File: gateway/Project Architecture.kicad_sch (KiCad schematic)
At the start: 0 parts

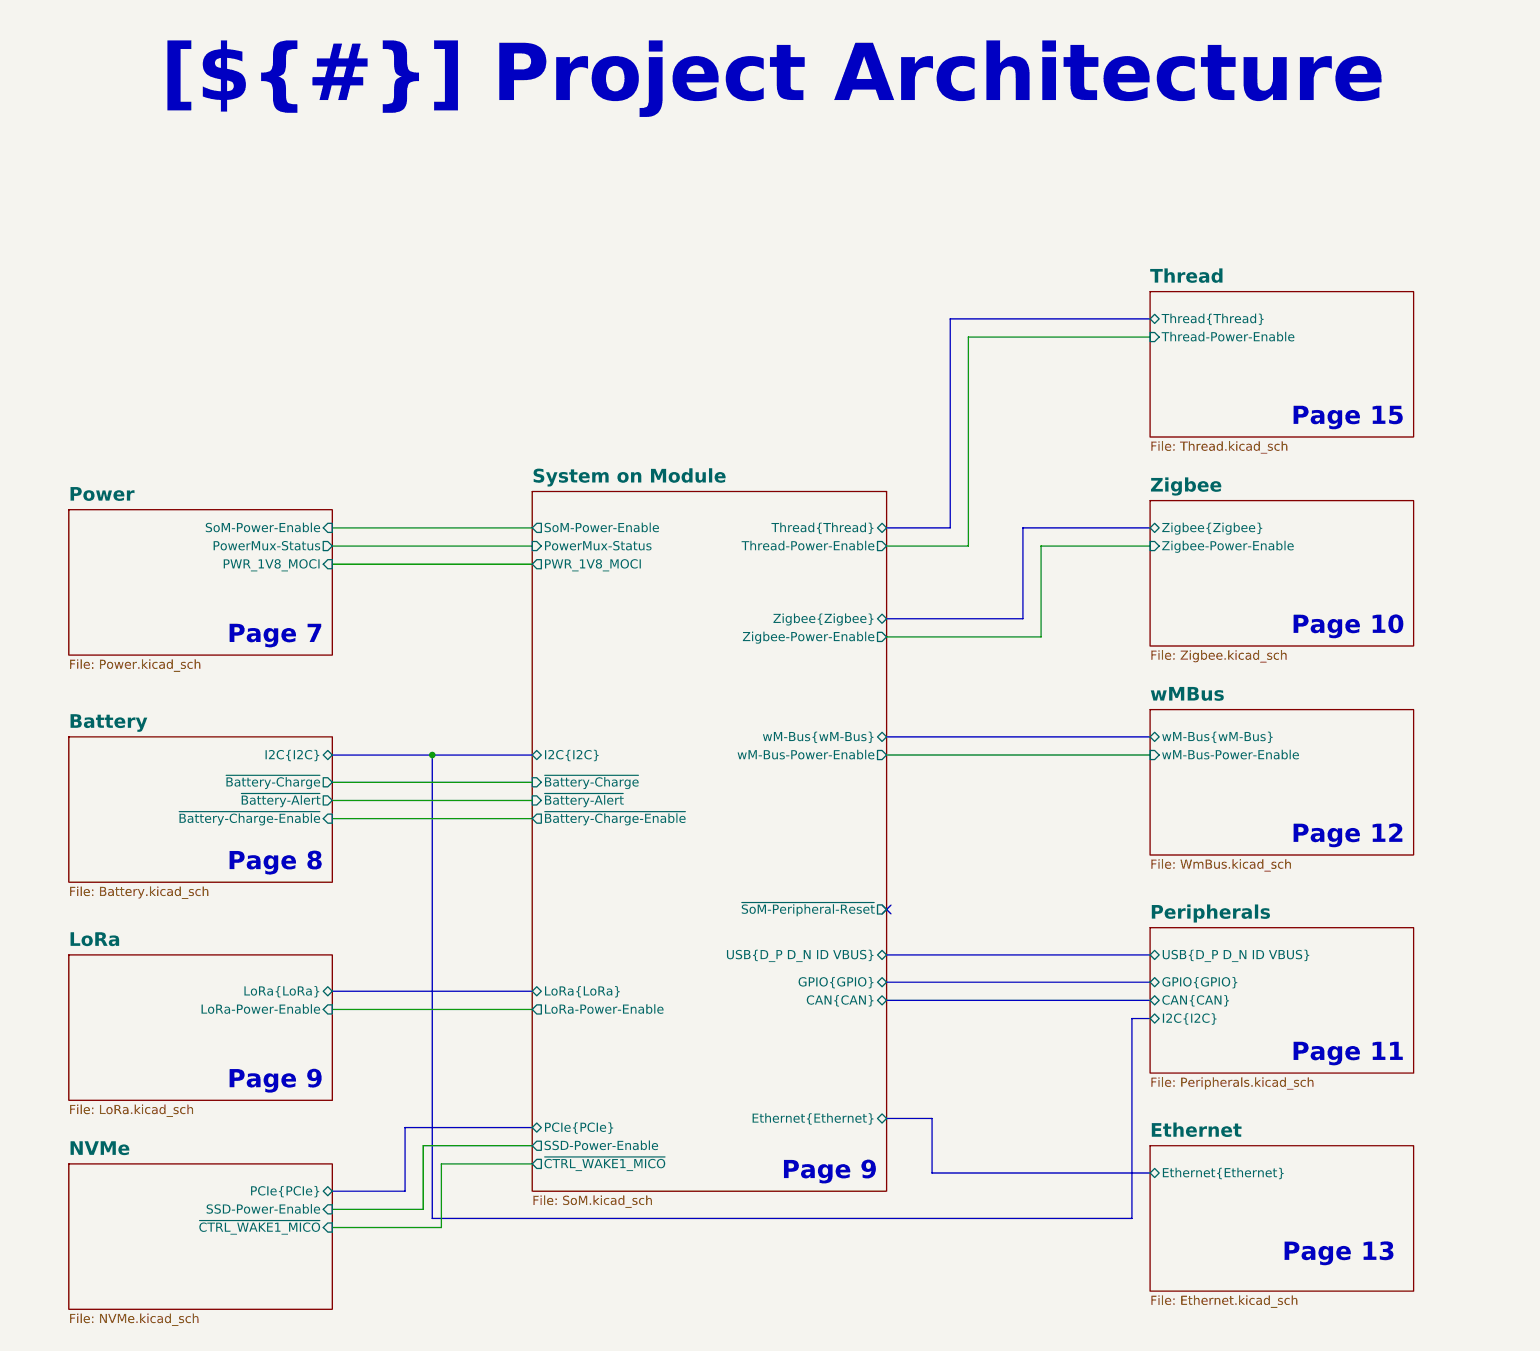
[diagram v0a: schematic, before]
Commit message: Add INA219 for current measurement
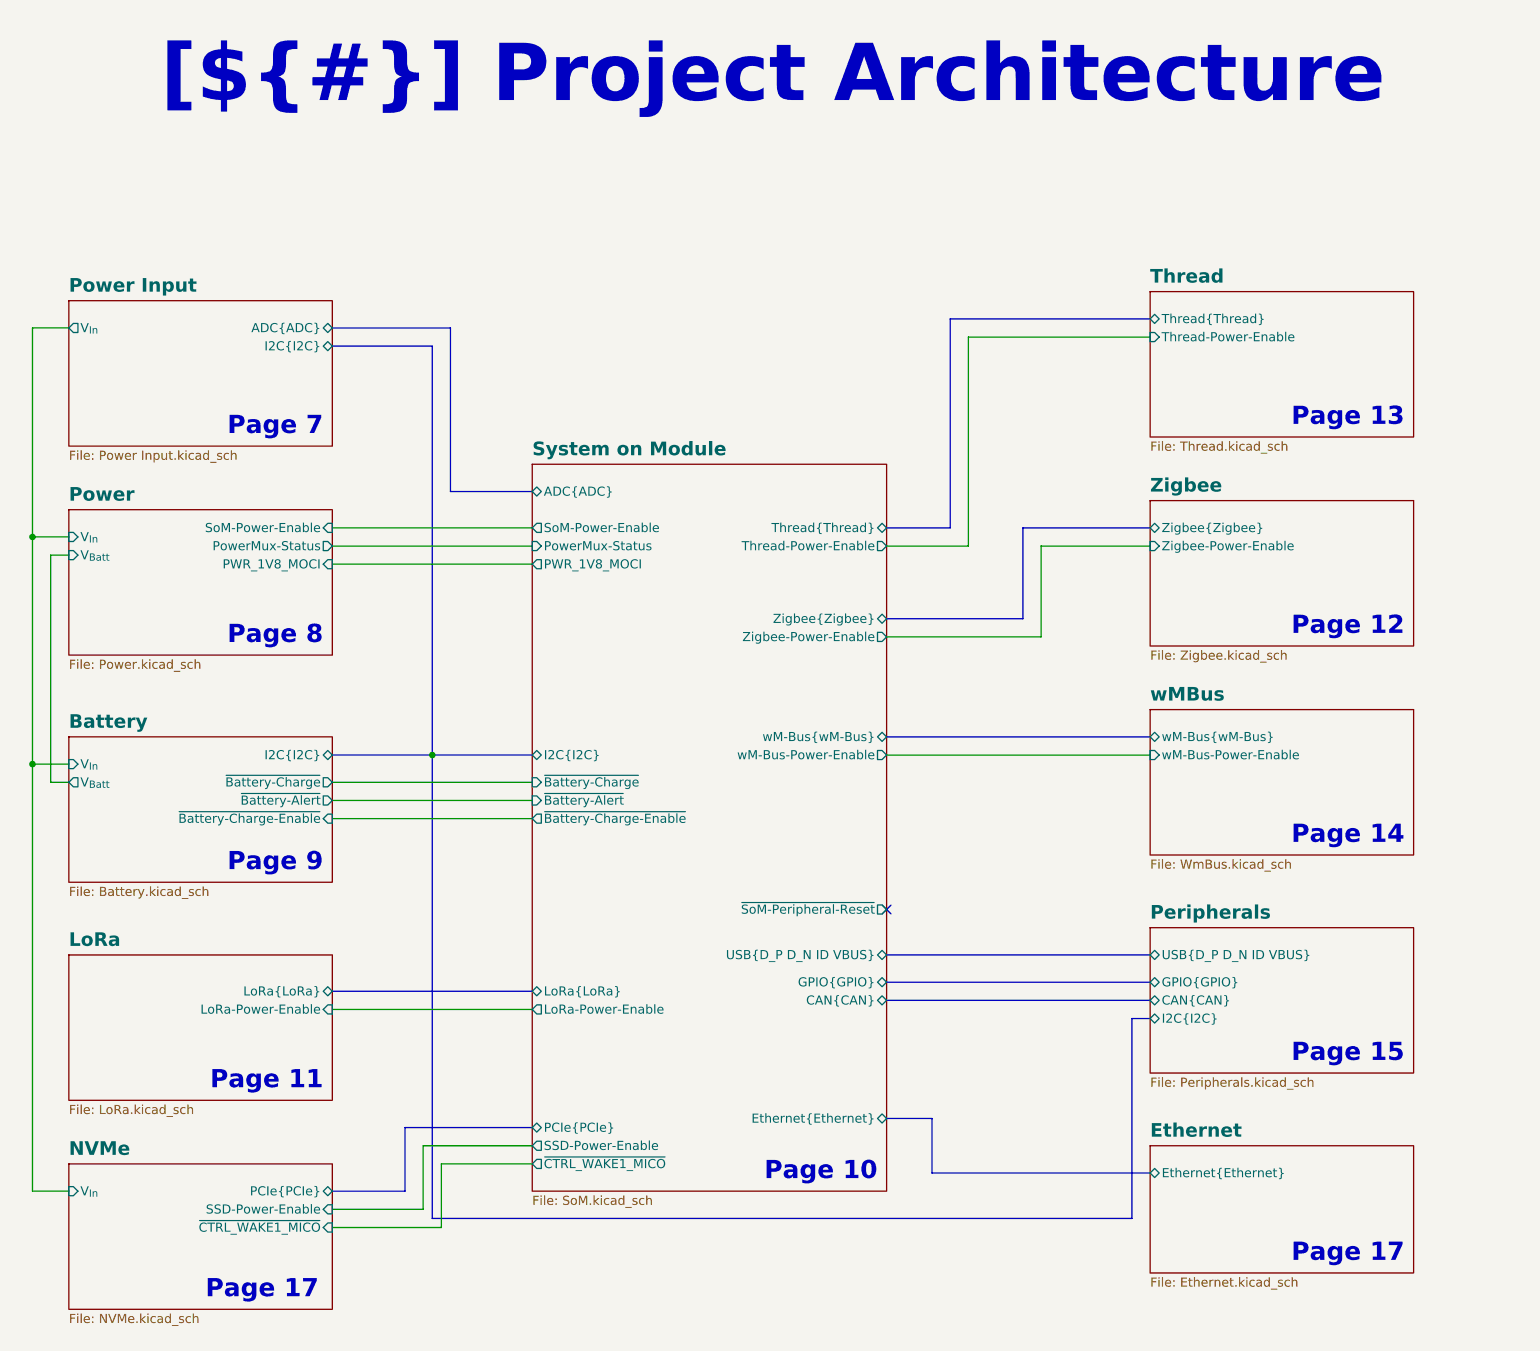
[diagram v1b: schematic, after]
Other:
- added sheet Power Input (Power Input.kicad_sch)
- sheet Battery ports: added V_{Batt}, V_{In}; removed none
- sheet NVMe ports: added V_{In}; removed none
- sheet Power ports: added V_{Batt}, V_{In}; removed none
- sheet System on Module ports: added ADC{ADC}; removed none
- note added: "Page 14"
- note added: "Page 17"

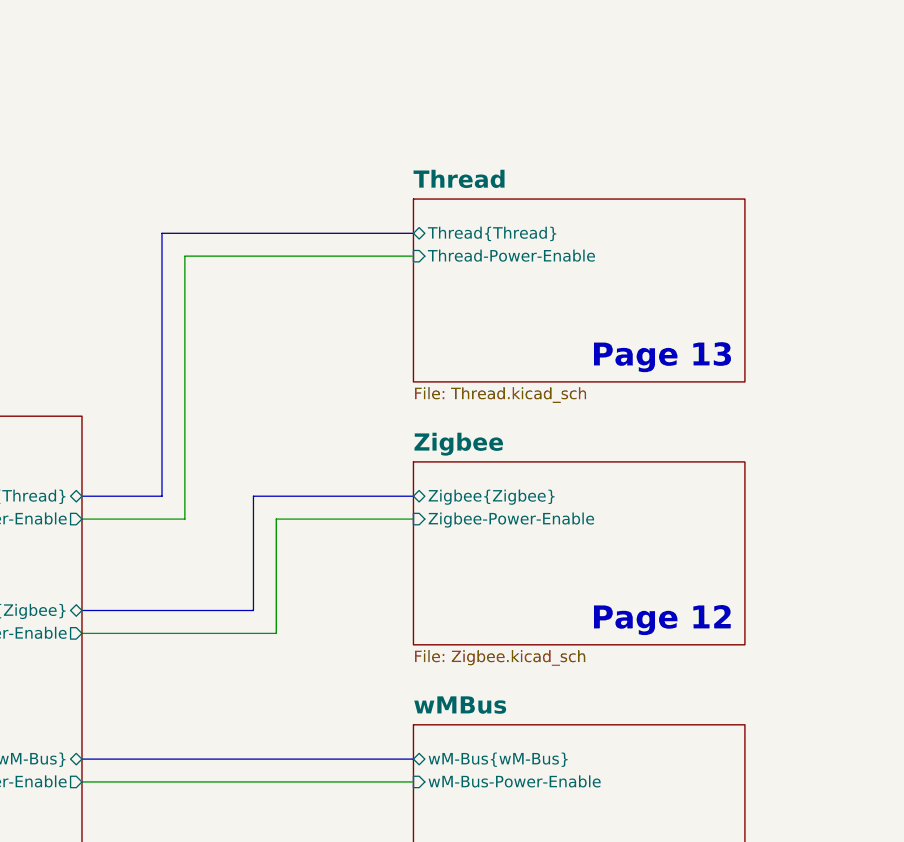
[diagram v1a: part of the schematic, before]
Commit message: Improving Thread
- Add boot signal for Thread MCU
- Add debug LED for nRF5340
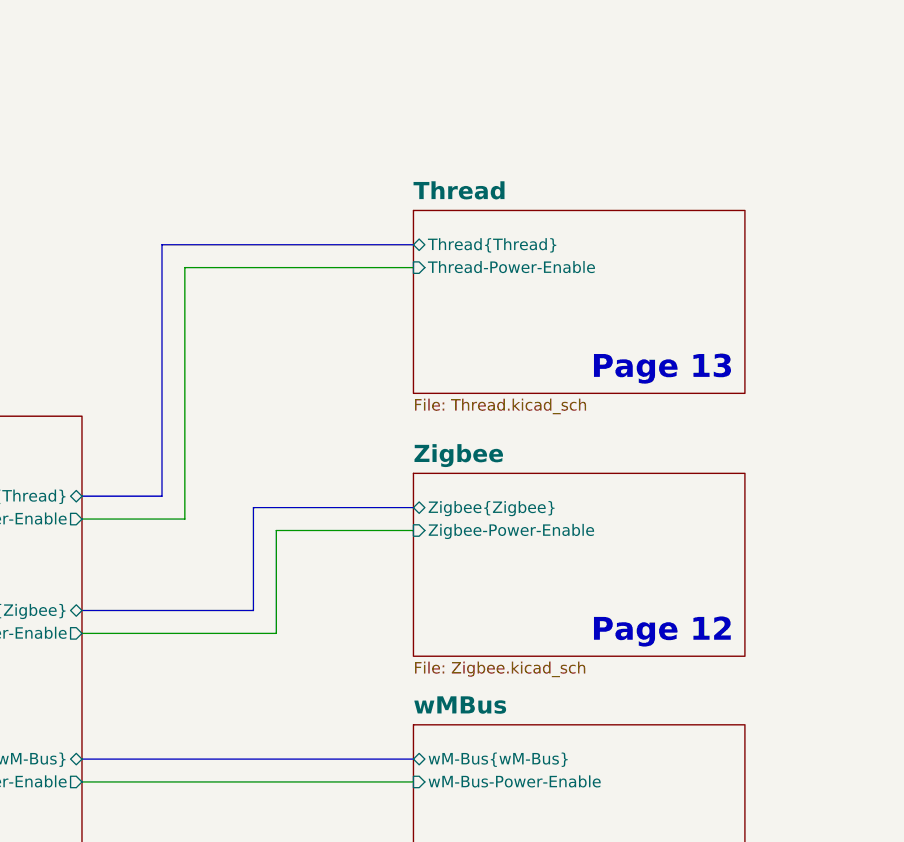
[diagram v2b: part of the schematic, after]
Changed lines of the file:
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@@
 	(text "Page 12"
 		(exclude_from_sim no)
-		(at 298.45 101.6 0)
+		(at 298.45 102.87 0)
 		(effects
 			(font
@@
 	(text "Page 13"
 		(exclude_from_sim no)
-		(at 298.45 72.39 0)
+		(at 298.45 73.66 0)
 		(effects
 			(font
@@
 	(bus
 		(pts
-			(xy 234.95 57.15) (xy 262.89 57.15)
+			(xy 234.95 58.42) (xy 262.89 58.42)
 		)
 		(stroke
@@
 	(wire
 		(pts
-			(xy 237.49 59.69) (xy 237.49 88.9)
+			(xy 237.49 60.96) (xy 237.49 88.9)
 		)
 		(stroke
@@
 	(wire
 		(pts
-			(xy 262.89 59.69) (xy 237.49 59.69)
+			(xy 262.89 60.96) (xy 237.49 60.96)
 		)
 		(stroke
@@
 	(wire
 		(pts
-			(xy 247.65 88.9) (xy 262.89 88.9)
+			(xy 247.65 90.17) (xy 262.89 90.17)
 		)
 		(stroke
@@
 	(bus
 		(pts
-			(xy 245.11 86.36) (xy 262.89 86.36)
+			(xy 245.11 87.63) (xy 262.89 87.63)
 		)
 		(stroke
@@
 	(wire
 		(pts
-			(xy 247.65 101.6) (xy 247.65 88.9)
+			(xy 247.65 101.6) (xy 247.65 90.17)
 		)
 		(stroke
@@
 	(bus
 		(pts
-			(xy 245.11 99.06) (xy 245.11 86.36)
-		)
-		(stroke
-			(width 0)
-			(type default)
-		)
-	)
-	(bus
-		(pts
-			(xy 234.95 86.36) (xy 234.95 57.15)
+			(xy 245.11 99.06) (xy 245.11 87.63)
+		)
+		(stroke
+			(width 0)
+			(type default)
+		)
+	)
+	(bus
+		(pts
+			(xy 234.95 86.36) (xy 234.95 58.42)
 		)
 		(stroke
@@
 	)
 	(sheet
-		(at 262.89 53.34)
+		(at 262.89 54.61)
 		(size 36.83 20.32)
 		(exclude_from_sim no)
@@
 		)
 		(property "Sheetname" "Thread"
-			(at 262.89 52.3109 0)
+			(at 262.89 53.5809 0)
 			(show_name no)
 			(do_not_autoplace no)
@@
 		)
 		(property "Sheetfile" "Thread.kicad_sch"
-			(at 262.89 74.2446 0)
+			(at 262.89 75.5146 0)
 			(show_name no)
 			(do_not_autoplace no)
@@
 		)
 		(pin "Thread{Thread}" bidirectional
-			(at 262.89 57.15 180)
+			(at 262.89 58.42 180)
 			(effects
 				(font
@@
 		)
 		(pin "Thread-Power-Enable" input
-			(at 262.89 59.69 180)
+			(at 262.89 60.96 180)
 			(effects
 				(font
@@
 	)
 	(sheet
-		(at 262.89 82.55)
+		(at 262.89 83.82)
 		(size 36.83 20.32)
 		(exclude_from_sim no)
@@
 		)
 		(property "Sheetname" "Zigbee"
-			(at 262.89 81.5209 0)
+			(at 262.89 82.7909 0)
 			(show_name no)
 			(do_not_autoplace no)
@@
 		)
 		(property "Sheetfile" "Zigbee.kicad_sch"
-			(at 262.89 103.4546 0)
+			(at 262.89 104.7246 0)
 			(show_name no)
 			(do_not_autoplace no)
@@
 		)
 		(pin "Zigbee{Zigbee}" bidirectional
-			(at 262.89 86.36 180)
+			(at 262.89 87.63 180)
 			(effects
 				(font
@@
 		)
 		(pin "Zigbee-Power-Enable" input
-			(at 262.89 88.9 180)
-			(effects
-				(font
+			(at 262.89 90.17 180)
+			(effects
+				(font

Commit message: Working on PCB
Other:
- sheet Ethernet ports: added AT-DET, PoE; removed none
- sheet Power ports: added Backup-Status; removed PowerMux-Status
- sheet Power Input ports: added Input-Status, PoE; removed none
- sheet System on Module ports: added AT-DET, Backup-Status, Input-Status; removed PowerMux-Status
- sheet wMBus: file WmBus.kicad_sch -> wMBus.kicad_sch
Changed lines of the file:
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@@
+		)
+	)
+	(wire
+		(pts
+			(xy 148.59 63.5) (xy 160.02 63.5)
+		)
+		(stroke
+			(width 0)
+			(type default)
 		)
 	)
@@
 	(wire
 		(pts
+			(xy 160.02 83.82) (xy 176.53 83.82)
+		)
+		(stroke
+			(width 0)
+			(type default)
+		)
+	)
+	(wire
+		(pts
 			(xy 237.49 88.9) (xy 226.06 88.9)
 		)
@@
 	(wire
 		(pts
-			(xy 111.76 58.42) (xy 106.68 58.42)
-		)
-		(stroke
-			(width 0)
-			(type default)
-		)
-	)
-	(bus
-		(pts
-			(xy 165.1 58.42) (xy 165.1 81.28)
-		)
-		(stroke
-			(width 0)
-			(type default)
-		)
-	)
-	(wire
-		(pts
-			(xy 106.68 58.42) (xy 106.68 87.63)
+			(xy 111.76 60.96) (xy 106.68 60.96)
+		)
+		(stroke
+			(width 0)
+			(type default)
+		)
+	)
+	(bus
+		(pts
+			(xy 165.1 58.42) (xy 165.1 77.47)
+		)
+		(stroke
+			(width 0)
+			(type default)
+		)
+	)
+	(wire
+		(pts
+			(xy 226.06 171.45) (xy 233.68 171.45)
+		)
+		(stroke
+			(width 0)
+			(type default)
+		)
+	)
+	(bus
+		(pts
+			(xy 238.76 154.94) (xy 262.89 154.94)
+		)
+		(stroke
+			(width 0)
+			(type default)
+		)
+	)
+	(wire
+		(pts
+			(xy 160.02 63.5) (xy 160.02 83.82)
+		)
+		(stroke
+			(width 0)
+			(type default)
+		)
+	)
+	(wire
+		(pts
+			(xy 106.68 60.96) (xy 106.68 87.63)
 		)
 		(stroke
@@
 	(wire
 		(pts
+			(xy 233.68 179.07) (xy 262.89 179.07)
+		)
+		(stroke
+			(width 0)
+			(type default)
+		)
+	)
+	(wire
+		(pts
 			(xy 106.68 179.07) (xy 106.68 119.38)
 		)
@@
 	(bus
 		(pts
-			(xy 226.06 168.91) (xy 232.41 168.91)
+			(xy 226.06 168.91) (xy 236.22 168.91)
 		)
 		(stroke
@@
 	(bus
 		(pts
+			(xy 238.76 182.88) (xy 238.76 154.94)
+		)
+		(stroke
+			(width 0)
+			(type default)
+		)
+	)
+	(bus
+		(pts
 			(xy 162.56 118.11) (xy 176.53 118.11)
 		)
@@
 		)
 	)
-	(bus
-		(pts
-			(xy 260.35 154.94) (xy 262.89 154.94)
-		)
-		(stroke
-			(width 0)
-			(type default)
-		)
-	)
-	(bus
-		(pts
-			(xy 260.35 182.88) (xy 260.35 154.94)
-		)
-		(stroke
-			(width 0)
-			(type default)
-		)
-	)
 	(wire
 		(pts
@@
 		)
 	)
-	(bus
-		(pts
-			(xy 232.41 176.53) (xy 262.89 176.53)
-		)
-		(stroke
-			(width 0)
-			(type default)
-		)
-	)
-	(bus
-		(pts
-			(xy 162.56 182.88) (xy 260.35 182.88)
+	(wire
+		(pts
+			(xy 111.76 58.42) (xy 104.14 58.42)
+		)
+		(stroke
+			(width 0)
+			(type default)
+		)
+	)
+	(bus
+		(pts
+			(xy 236.22 176.53) (xy 262.89 176.53)
+		)
+		(stroke
+			(width 0)
+			(type default)
+		)
+	)
+	(bus
+		(pts
+			(xy 162.56 182.88) (xy 238.76 182.88)
 		)
 		(stroke
@@
 	(bus
 		(pts
-			(xy 232.41 168.91) (xy 232.41 176.53)
+			(xy 236.22 168.91) (xy 236.22 176.53)
+		)
+		(stroke
+			(width 0)
+			(type default)
+		)
+	)
+	(wire
+		(pts
+			(xy 104.14 199.39) (xy 260.35 199.39)
 		)
 		(stroke
@@
 	(bus
 		(pts
-			(xy 165.1 81.28) (xy 176.53 81.28)
+			(xy 165.1 77.47) (xy 176.53 77.47)
 		)
 		(stroke
@@
 		)
 	)
+	(wire
+		(pts
+			(xy 233.68 171.45) (xy 233.68 179.07)
+		)
+		(stroke
+			(width 0)
+			(type default)
+		)
+	)
 	(bus
 		(pts
@@
 	(wire
 		(pts
+			(xy 262.89 181.61) (xy 260.35 181.61)
+		)
+		(stroke
+			(width 0)
+			(type default)
+		)
+	)
+	(wire
+		(pts
 			(xy 106.68 87.63) (xy 111.76 87.63)
 		)
@@
 		)
 	)
+	(wire
+		(pts
+			(xy 104.14 58.42) (xy 104.14 199.39)
+		)
+		(stroke
+			(width 0)
+			(type default)
+		)
+	)
 	(bus
 		(pts
@@
 		(pts
 			(xy 234.95 86.36) (xy 234.95 58.42)
+		)
+		(stroke
+			(width 0)
+			(type default)
+		)
+	)
+	(wire
+		(pts
+			(xy 260.35 181.61) (xy 260.35 199.39)
 		)
 		(stroke
@@
 		)
 		(pin "V_{In}" output
-			(at 111.76 58.42 180)
+			(at 111.76 60.96 180)
 			(effects
 				(font
@@
 				)
 				(justify right)
+			)
+		)
+		(pin "Input-Status" output
+			(at 148.59 63.5 0)
+			(effects
+				(font
+					(size 1.27 1.27)
+				)
+				(justify right)
+			)
+		)
+		(pin "PoE" input
+			(at 111.76 58.42 180)
+			(effects
+				(font
+					(size 1.27 1.27)
+				)
+				(justify left)
 			)
 		)
@@
 			)
 		)
-		(property "Sheetfile" "WmBus.kicad_sch"
+		(property "Sheetfile" "wMBus.kicad_sch"
 			(at 262.89 132.6646 0)
 			(show_name no)
@@
 			)
 		)
+		(pin "PoE" output
+			(at 262.89 181.61 180)
+			(effects
+				(font
+					(size 1.27 1.27)
+				)
+				(justify left)
+			)
+		)
+		(pin "AT-DET" output
+			(at 262.89 179.07 180)
+			(effects
+				(font
+					(size 1.27 1.27)
+				)
+				(justify left)
+			)
+		)
 		(instances
 			(project "Gateway"
@@
 	)
 	(sheet
-		(at 176.53 77.47)
-		(size 49.53 101.6)
+		(at 176.53 74.93)
+		(size 49.53 104.14)
 		(exclude_from_sim no)
 		(in_bom yes)
@@
 		)
 		(property "Sheetname" "System on Module"
-			(at 176.53 76.4409 0)
+			(at 176.53 73.9009 0)
 			(show_name no)
 			(do_not_autoplace no)
@@
 			)
 		)
-		(pin "PowerMux-Status" input
+		(pin "Backup-Status" input
 			(at 176.53 88.9 180)
 			(effects
@@
 		)
 		(pin "ADC{ADC}" bidirectional
-			(at 176.53 81.28 180)
-			(effects
-				(font
-					(size 1.27 1.27)
-				)
-				(justify left)
+			(at 176.53 77.47 180)
+			(effects
+				(font
+					(size 1.27 1.27)
+				)
+				(justify left)
+			)
+		)
+		(pin "Input-Status" input
+			(at 176.53 83.82 180)
+			(effects
+				(font
+					(size 1.27 1.27)
+				)
+				(justify left)
+			)
+		)
+		(pin "AT-DET" input
+			(at 226.06 171.45 0)
+			(effects
+				(font
+					(size 1.27 1.27)
+				)
+				(justify right)
 			)
 		)
@@
 			)
 		)
-		(pin "PowerMux-Status" output
+		(pin "Backup-Status" output
 			(at 148.59 88.9 0)
 			(effects

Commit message: Replace battery charger with BQ25300
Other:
- sheet Battery ports: added Battery-Charge-Enable; removed ~{Battery-Charge-Enable}
- sheet System on Module ports: added Battery-Charge-Enable; removed ~{Battery-Charge-Enable}
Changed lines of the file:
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@@
 			)
 		)
-		(pin "~{Battery-Charge-Enable}" input
+		(pin "Battery-Charge-Enable" input
 			(at 148.59 127 0)
 			(effects
@@
 			)
 		)
-		(pin "~{Battery-Charge-Enable}" output
+		(pin "Battery-Charge-Enable" output
 			(at 176.53 127 180)
 			(effects

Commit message: Working on revision 1.0.0
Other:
- sheet Battery ports: added Battery-Backup-Enable; removed none
- sheet Power ports: added PowerMux-Status; removed Backup-Status
- sheet System on Module ports: added Battery-Backup-Enable, PowerMux-Status; removed Backup-Status
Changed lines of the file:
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@@
+	(wire
+		(pts
+			(xy 148.59 129.54) (xy 176.53 129.54)
+		)
+		(stroke
+			(width 0)
+			(type default)
+		)
+	)
 	(wire
 		(pts
@@
 			)
 		)
+		(pin "Battery-Backup-Enable" input
+			(at 148.59 129.54 0)
+			(effects
+				(font
+					(size 1.27 1.27)
+				)
+				(justify right)
+			)
+		)
 		(instances
 			(project "Gateway"
@@
 			)
 		)
-		(pin "Backup-Status" input
+		(pin "PowerMux-Status" input
 			(at 176.53 88.9 180)
 			(effects
@@
 				)
 				(justify right)
+			)
+		)
+		(pin "Battery-Backup-Enable" output
+			(at 176.53 129.54 180)
+			(effects
+				(font
+					(size 1.27 1.27)
+				)
+				(justify left)
 			)
 		)
@@
 			)
 		)
-		(pin "Backup-Status" output
-			(at 148.59 88.9 0)
-			(effects
-				(font
-					(size 1.27 1.27)
-				)
-				(justify right)
-			)
-		)
 		(pin "PWR_1V8_MOCI" input
 			(at 148.59 91.44 0)
@@
 			)
 		)
+		(pin "PowerMux-Status" output
+			(at 148.59 88.9 0)
+			(effects
+				(font
+					(size 1.27 1.27)
+				)
+				(justify right)
+			)
+		)
